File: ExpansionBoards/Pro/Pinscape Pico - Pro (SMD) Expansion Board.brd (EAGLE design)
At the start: 170.6 x 108 mm, 213 parts, among them IC1 UCC27523D, IC10 UCC27523D, IC11 UCC27523D, IC12 UCC27523D, IC13 UCC27523D, IC14 UCC27523D, IC15 TLC59116FIRHBR, IC16 TLC59116FIRHBR, IC17 TLC59116FIRHBR, IC18 TLC59116FIRHBR, IC19 ULN2803ADWR, IC2 UCC27523D, IC20 ULN2803ADWR, IC21 ULN2803ADWR, IC22 ULN2803ADWR, IC23 ULN2803ADWR, IC24 SN74HC165PWR, IC25 SN74HC165PWR, IC26 SN74HC165PWR, IC27 SN74HC165PWR, IC28 LIS3DHTR, IC29 SN74LVC1G175DCKR, IC3 UCC27523D, IC30 APX809S-29SA-7, IC31 LTV-827S, IC32 ADS1115IDGSR, IC33 TLV75733PDBVR, IC34 RV-3032-C7, IC4 UCC27523D, IC5 UCC27523D, IC6 UCC27523D, IC7 UCC27523D, IC8 UCC27523D, IC9 UCC27523D, J1 640445-6, J10 1-640456-0, J11 1-640456-0, J12 1-640456-0, J13 640445-5, J14 640445-9, J15 640445-9, J16 640445-9, J2 30316-6002HB, J3 1-640456-0, J4 640456-9, J5 640456-9, J6 640454-2, J7 215079-4, J8 30308-6002HB, J9 1-640456-0, Q1 BUK7K89-100EX, Q10 BUK7K89-100EX, Q11 BUK7K89-100EX, Q12 BUK7K89-100EX, Q13 BUK7K89-100EX, Q14 BUK7K89-100EX, Q15 UMA5NTR, Q16 UMA5NTR, Q17 UMA5NTR, Q18 UMA5NTR, Q19 UMA5NTR, Q2 BUK7K89-100EX, Q20 UMA5NTR, Q21 UMA5NTR, Q22 UMA5NTR, Q23 UMA5NTR, Q24 UMA5NTR, Q25 UMA5NTR, Q26 UMA5NTR, Q27 DSS8110Y-7, Q3 BUK7K89-100EX, Q4 BUK7K89-100EX, Q5 BUK7K89-100EX, Q6 BUK7K89-100EX, Q7 BUK7K89-100EX, Q8 BUK7K89-100EX, Q9 BUK7K89-100EX, SW1 TS-1187A-B-A-B, U1 BAT-HLD-001-THM

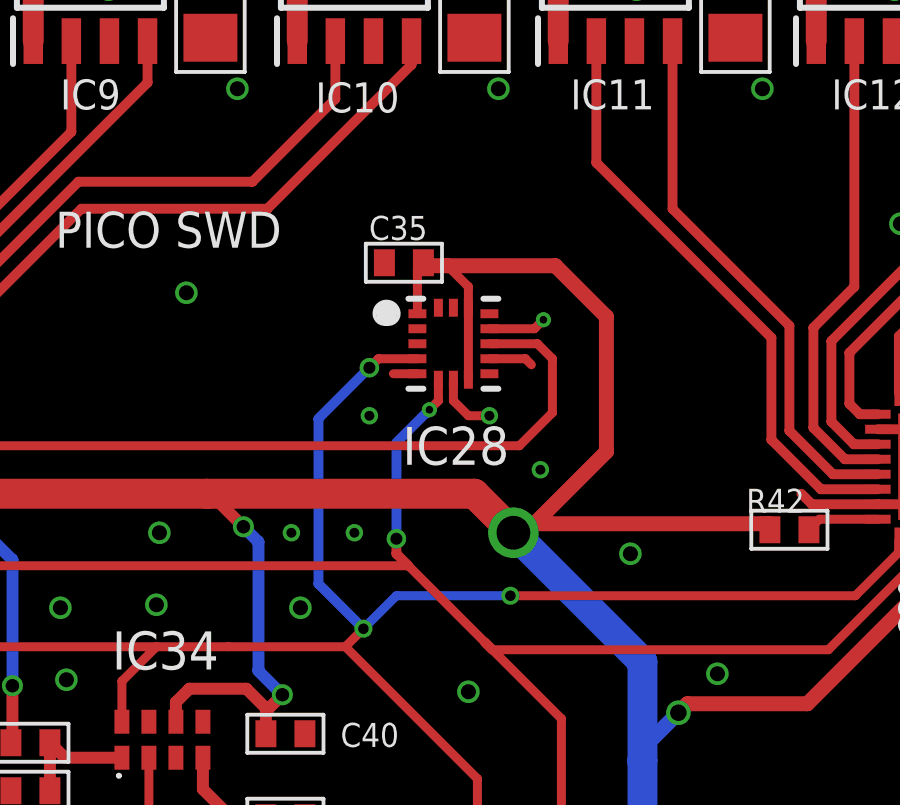
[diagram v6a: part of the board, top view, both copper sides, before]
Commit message: Update Pro and KL25Z adapter boards to make LIS3DH footprint compatible with LIS3DSH
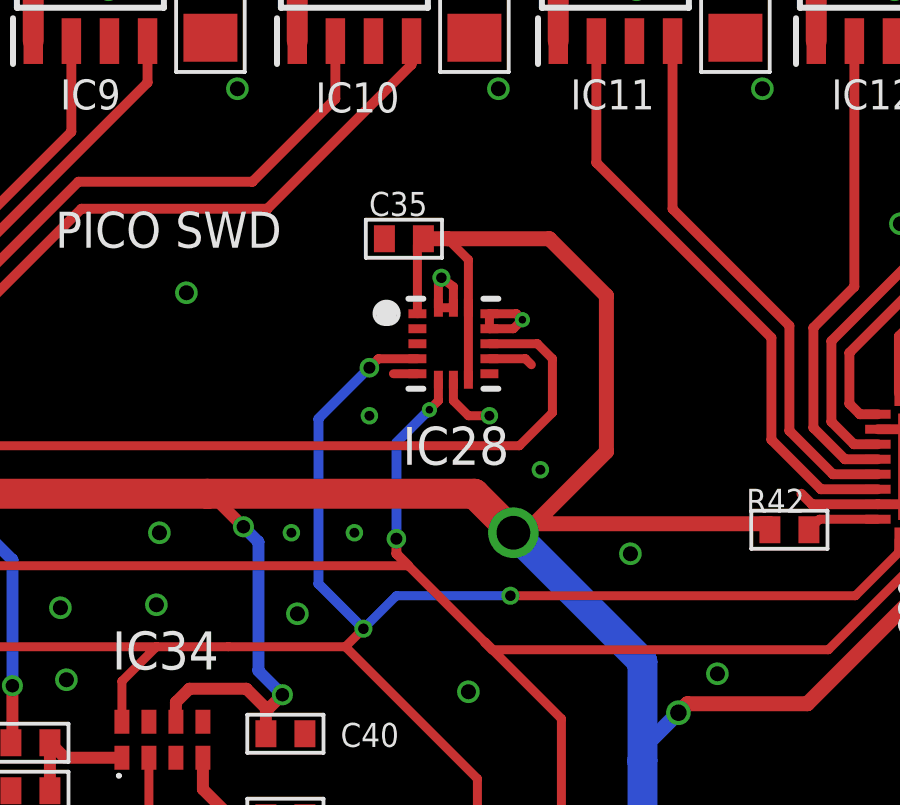
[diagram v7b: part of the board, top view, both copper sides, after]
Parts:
- moved C35 0.80 mm to (95.5, 68.4)
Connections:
- net GND: now also IC28.13, IC28.15, IC28.16
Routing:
- net GND: track 113.2 -> 117.0 mm, vias 312 -> 313
- net 3V3_PERIPHERAL: track 359.3 -> 361.7 mm
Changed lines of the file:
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@@
 <layer number="98" name="Guide" color="6" fill="1" visible="no" active="no"/>
 <layer number="99" name="SpiceOrder" color="5" fill="1" visible="no" active="no"/>
-<layer number="100" name="US-Transistor" color="7" fill="1" visible="no" active="yes"/>
-<layer number="101" name="EU-Transistor" color="7" fill="1" visible="no" active="yes"/>
+<layer number="100" name="US-Transistor" color="7" fill="1" visible="yes" active="yes"/>
+<layer number="101" name="EU-Transistor" color="7" fill="1" visible="yes" active="yes"/>
 <layer number="102" name="Vscore" color="7" fill="1" visible="no" active="yes"/>
 <layer number="103" name="fp3" color="7" fill="1" visible="no" active="yes"/>
@@
 <attribute name="VALUE" x="83.386" y="18.23" size="0.8" layer="27" rot="R90" align="center"/>
 </element>
-<element name="C35" library="rcl" package="C0402" value="0.1uF" x="95.45" y="67.6" smashed="yes" rot="R180">
-<attribute name="NAME" x="95.26" y="68.76" size="0.8" layer="25" align="center"/>
+<element name="C35" library="rcl" package="C0402" value="0.1uF" x="95.45" y="68.4" smashed="yes" rot="R180">
+<attribute name="NAME" x="95.26" y="69.56" size="0.8" layer="25" align="center"/>
 </element>
 <element name="R31" library="rcl" package="R0603" value="2R5" x="99.4" y="14.4" smashed="yes" rot="R90">
@@
 <attribute name="MOUSER_PART_NUMBER" value="511-LIS3DHTR" x="97.1" y="64.9" size="1" layer="27" ratio="15" display="off"/>
 <attribute name="NAME" x="97.181" y="61.5" size="1.27" layer="25" rot="R180" align="center"/>
-<attribute name="VALUE" x="99.4" y="65.519" size="0.7" layer="27" rot="R90" align="center"/>
+<attribute name="VALUE" x="92.881" y="65" size="0.7" layer="27" rot="R180" align="center"/>
 </element>
 <element name="IC31" library="SamacSys_Parts" package="SOP254P1016X460-8N" value="LTV-827S" x="44.1" y="37.6" smashed="yes" rot="R180">
@@
 <via x="52.5" y="14" extent="1-16" drill="0.254"/>
 <via x="94.3" y="42" extent="1-16" drill="0.5"/>
-<via x="92" y="56.1" extent="1-16" drill="0.5"/>
+<via x="91.9" y="55.9" extent="1-16" drill="0.5"/>
 <via x="105.7" y="39.9" extent="1-16" drill="0.3" diameter="0.7"/>
 <via x="101.7" y="39.8" extent="1-16" drill="0.3" diameter="0.7"/>
@@
 <via x="98.3" y="62.5" extent="1-16" drill="0.33"/>
 <via x="100" y="60.7" extent="1-16" drill="0.33"/>
-<wire x1="98.3" y1="65.4" x2="99.8" y2="65.4" width="0.3" layer="1"/>
+<wire x1="98.3" y1="65.4" x2="99.1" y2="65.4" width="0.3" layer="1"/>
 <wire x1="97.1" y1="63.7" x2="97.1" y2="63" width="0.3" layer="1"/>
 <wire x1="97.1" y1="63" x2="97.6" y2="62.5" width="0.3" layer="1"/>
-<wire x1="99.8" y1="65.4" x2="100.1" y2="65.7" width="0.3" layer="1"/>
-<via x="100.1" y="65.7" extent="1-16" drill="0.254"/>
+<wire x1="99.1" y1="65.4" x2="99.4" y2="65.7" width="0.3" layer="1"/>
+<via x="99.4" y="65.7" extent="1-16" drill="0.254"/>
 <wire x1="98.3" y1="62.5" x2="97.6" y2="62.5" width="0.3" layer="1"/>
 <contactref element="J1" pad="2"/>
@@
 <contactref element="R31" pad="1"/>
 <contactref element="D2" pad="1"/>
+<contactref element="IC28" pad="13"/>
+<contactref element="IC28" pad="15"/>
+<contactref element="IC28" pad="16"/>
+<wire x1="97.1" y1="66.1" x2="96.6" y2="66.1" width="0.3" layer="1"/>
+<via x="96.7" y="67.1" extent="1-16" drill="0.35"/>
+<wire x1="96.6" y1="66.1" x2="96.6" y2="67" width="0.3" layer="1"/>
+<wire x1="96.6" y1="67" x2="96.7" y2="67.1" width="0.3" layer="1"/>
+<wire x1="97.1" y1="66.1" x2="97.1" y2="66.8" width="0.3" layer="1"/>
+<wire x1="97.1" y1="66.8" x2="96.7" y2="67.1" width="0.3" layer="1"/>
+<wire x1="98.3" y1="65.9" x2="98.3" y2="65.4" width="0.3" layer="1"/>
+<wire x1="98.3" y1="65.9" x2="99.2" y2="65.9" width="0.3" layer="1"/>
+<wire x1="99.2" y1="65.9" x2="99.4" y2="65.7" width="0.3" layer="1"/>
 </signal>
 <signal name="5V">
@@
 <contactref element="IC28" pad="1"/>
 <contactref element="IC28" pad="14"/>
-<wire x1="97.6" y1="66.1" x2="97.6" y2="66.8" width="0.3" layer="1"/>
-<wire x1="95.9" y1="65.9" x2="95.9" y2="67.4" width="0.3" layer="1"/>
-<wire x1="95.9" y1="67.4" x2="96.1" y2="67.6" width="0.3" layer="1"/>
-<wire x1="96.1" y1="67.6" x2="96.1" y2="67.5" width="0.3" layer="1"/>
-<wire x1="102.2" y1="61.3" x2="102.2" y2="65.8" width="0.5" layer="1"/>
-<wire x1="96.1" y1="67.5" x2="96.9" y2="67.5" width="0.5" layer="1"/>
-<wire x1="96.9" y1="67.5" x2="100.5" y2="67.5" width="0.5" layer="1"/>
-<wire x1="97.6" y1="66.8" x2="96.9" y2="67.5" width="0.3" layer="1"/>
+<wire x1="95.9" y1="65.9" x2="95.9" y2="68.2" width="0.3" layer="1"/>
+<wire x1="95.9" y1="68.2" x2="96.1" y2="68.4" width="0.3" layer="1"/>
+<wire x1="102.2" y1="61.3" x2="102.2" y2="66.5" width="0.5" layer="1"/>
+<wire x1="96.1" y1="68.4" x2="96.9" y2="68.4" width="0.5" layer="1"/>
 <contactref element="R39" pad="2"/>
 <contactref element="R42" pad="2"/>
 <contactref element="R43" pad="2"/>
 <contactref element="R44" pad="2"/>
+<wire x1="96.9" y1="68.4" x2="100.3" y2="68.4" width="0.5" layer="1"/>
 <wire x1="48.05" y1="63.6" x2="48.05" y2="61.95" width="0.33" layer="1"/>
 <wire x1="109.95" y1="42.3" x2="104.4" y2="42.3" width="0.33" layer="1"/>
@@
 <contactref element="LED2" pad="2"/>
 <contactref element="IC28" pad="8"/>
-<wire x1="100.5" y1="67.5" x2="102.2" y2="65.8" width="0.5" layer="1"/>
 <wire x1="107.65" y1="58.9" x2="99.4" y2="58.9" width="0.5" layer="1"/>
 <wire x1="99.4" y1="58.9" x2="99.1" y2="58.6" width="0.5" layer="1"/>
@@
 <wire x1="40.1" y1="13.1" x2="38.59" y2="11.59" width="0.5" layer="16"/>
 <wire x1="38.59" y1="25.845675" x2="38.59" y2="38.41" width="1" layer="16"/>
+<wire x1="102.2" y1="66.5" x2="100.3" y2="68.4" width="0.5" layer="1"/>
+<wire x1="97.6" y1="66.1" x2="97.6" y2="67.7" width="0.3" layer="1"/>
+<wire x1="97.6" y1="67.7" x2="96.9" y2="68.4" width="0.3" layer="1"/>
 </signal>
 <signal name="/OUTCTL1">

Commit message: Exp boards: update gate resistors in BOMs
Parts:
- R10, R11, R12, R13, R14, R15, R16, R17, R18, R19, R20, R21, R22, R23, R24, R25, R26, R27, R28, R5, R6, R7, R8, R9: value 4R7 -> 200R
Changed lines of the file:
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@@
 <attribute name="VALUE" x="119.8" y="78.69" size="0.55" layer="27" rot="R180" align="center"/>
 </element>
-<element name="R21" library="resistor" package="R0603" value="4R7" x="101.3" y="83.1" smashed="yes" rot="R270">
+<element name="R21" library="resistor" package="R0603" value="200R" x="101.3" y="83.1" smashed="yes" rot="R270">
 <attribute name="NAME" x="101.37" y="85.284" size="0.8" layer="25" rot="R180" align="center"/>
 </element>
-<element name="R22" library="resistor" package="R0603" value="4R7" x="106.1" y="83.1" smashed="yes" rot="R270">
+<element name="R22" library="resistor" package="R0603" value="200R" x="106.1" y="83.1" smashed="yes" rot="R270">
 <attribute name="NAME" x="106.17" y="85.184" size="0.8" layer="25" rot="R180" align="center"/>
 </element>
-<element name="R23" library="resistor" package="R0603" value="4R7" x="109.9" y="83.1" smashed="yes" rot="R270">
+<element name="R23" library="resistor" package="R0603" value="200R" x="109.9" y="83.1" smashed="yes" rot="R270">
 <attribute name="NAME" x="109.87" y="85.184" size="0.8" layer="25" rot="R180" align="center"/>
 </element>
-<element name="R24" library="resistor" package="R0603" value="4R7" x="114.9" y="83.1" smashed="yes" rot="R270">
+<element name="R24" library="resistor" package="R0603" value="200R" x="114.9" y="83.1" smashed="yes" rot="R270">
 <attribute name="NAME" x="116.484" y="83.33" size="0.8" layer="25" rot="R90" align="center"/>
 </element>
-<element name="R25" library="resistor" package="R0603" value="4R7" x="118.6" y="83.1" smashed="yes" rot="R270">
+<element name="R25" library="resistor" package="R0603" value="200R" x="118.6" y="83.1" smashed="yes" rot="R270">
 <attribute name="NAME" x="118.57" y="85.184" size="0.8" layer="25" rot="R180" align="center"/>
 </element>
-<element name="R26" library="resistor" package="R0603" value="4R7" x="123.4" y="83.1" smashed="yes" rot="R270">
+<element name="R26" library="resistor" package="R0603" value="200R" x="123.4" y="83.1" smashed="yes" rot="R270">
 <attribute name="NAME" x="123.47" y="85.184" size="0.8" layer="25" rot="R180" align="center"/>
 </element>
-<element name="R27" library="resistor" package="R0603" value="4R7" x="127.3" y="83.1" smashed="yes" rot="R270">
+<element name="R27" library="resistor" package="R0603" value="200R" x="127.3" y="83.1" smashed="yes" rot="R270">
 <attribute name="NAME" x="127.37" y="85.184" size="0.8" layer="25" rot="R180" align="center"/>
 </element>
-<element name="R28" library="resistor" package="R0603" value="4R7" x="132.3" y="83.1" smashed="yes" rot="R270">
+<element name="R28" library="resistor" package="R0603" value="200R" x="132.3" y="83.1" smashed="yes" rot="R270">
 <attribute name="NAME" x="132.465" y="85.235" size="0.8" layer="25" align="center"/>
 </element>
-<element name="R13" library="resistor" package="R0603" value="4R7" x="66.5" y="83.1" smashed="yes" rot="R270">
+<element name="R13" library="resistor" package="R0603" value="200R" x="66.5" y="83.1" smashed="yes" rot="R270">
 <attribute name="NAME" x="66.37" y="85.084" size="0.8" layer="25" rot="R180" align="center"/>
 </element>
-<element name="R14" library="resistor" package="R0603" value="4R7" x="71.3" y="83.1" smashed="yes" rot="R270">
+<element name="R14" library="resistor" package="R0603" value="200R" x="71.3" y="83.1" smashed="yes" rot="R270">
 <attribute name="NAME" x="71.4" y="85.2" size="0.8" layer="25" rot="R180" align="center"/>
 </element>
-<element name="R15" library="resistor" package="R0603" value="4R7" x="75.1" y="83.1" smashed="yes" rot="R270">
+<element name="R15" library="resistor" package="R0603" value="200R" x="75.1" y="83.1" smashed="yes" rot="R270">
 <attribute name="NAME" x="75.07" y="85.184" size="0.8" layer="25" rot="R180" align="center"/>
 </element>
-<element name="R16" library="resistor" package="R0603" value="4R7" x="80" y="83.1" smashed="yes" rot="R270">
+<element name="R16" library="resistor" package="R0603" value="200R" x="80" y="83.1" smashed="yes" rot="R270">
 <attribute name="NAME" x="79.97" y="85.184" size="0.8" layer="25" rot="R180" align="center"/>
 </element>
-<element name="R17" library="resistor" package="R0603" value="4R7" x="83.9" y="83.1" smashed="yes" rot="R270">
+<element name="R17" library="resistor" package="R0603" value="200R" x="83.9" y="83.1" smashed="yes" rot="R270">
 <attribute name="NAME" x="84.07" y="85.184" size="0.8" layer="25" rot="R180" align="center"/>
 </element>
-<element name="R18" library="resistor" package="R0603" value="4R7" x="88.7" y="83.1" smashed="yes" rot="R270">
+<element name="R18" library="resistor" package="R0603" value="200R" x="88.7" y="83.1" smashed="yes" rot="R270">
 <attribute name="NAME" x="88.77" y="85.284" size="0.8" layer="25" rot="R180" align="center"/>
 </element>
-<element name="R19" library="resistor" package="R0603" value="4R7" x="92.6" y="83.1" smashed="yes" rot="R270">
+<element name="R19" library="resistor" package="R0603" value="200R" x="92.6" y="83.1" smashed="yes" rot="R270">
 <attribute name="NAME" x="92.57" y="85.184" size="0.8" layer="25" rot="R180" align="center"/>
 </element>
-<element name="R20" library="resistor" package="R0603" value="4R7" x="97.5" y="83.1" smashed="yes" rot="R270">
+<element name="R20" library="resistor" package="R0603" value="200R" x="97.5" y="83.1" smashed="yes" rot="R270">
 <attribute name="NAME" x="97.67" y="85.184" size="0.8" layer="25" rot="R180" align="center"/>
 </element>
-<element name="R5" library="resistor" package="R0603" value="4R7" x="32" y="83.1" smashed="yes" rot="R270">
+<element name="R5" library="resistor" package="R0603" value="200R" x="32" y="83.1" smashed="yes" rot="R270">
 <attribute name="NAME" x="32.165" y="85.235" size="0.8" layer="25" align="center"/>
 </element>
-<element name="R6" library="resistor" package="R0603" value="4R7" x="36.8" y="83.1" smashed="yes" rot="R270">
+<element name="R6" library="resistor" package="R0603" value="200R" x="36.8" y="83.1" smashed="yes" rot="R270">
 <attribute name="NAME" x="36.77" y="85.184" size="0.8" layer="25" rot="R180" align="center"/>
 </element>
-<element name="R7" library="resistor" package="R0603" value="4R7" x="40.4" y="83.1" smashed="yes" rot="R270">
+<element name="R7" library="resistor" package="R0603" value="200R" x="40.4" y="83.1" smashed="yes" rot="R270">
 <attribute name="NAME" x="40.77" y="85.084" size="0.8" layer="25" rot="R180" align="center"/>
 </element>
-<element name="R8" library="resistor" package="R0603" value="4R7" x="45.2" y="83.1" smashed="yes" rot="R270">
+<element name="R8" library="resistor" package="R0603" value="200R" x="45.2" y="83.1" smashed="yes" rot="R270">
 <attribute name="NAME" x="45.17" y="85.184" size="0.8" layer="25" rot="R180" align="center"/>
 </element>
-<element name="R9" library="resistor" package="R0603" value="4R7" x="49.2" y="83.1" smashed="yes" rot="R270">
+<element name="R9" library="resistor" package="R0603" value="200R" x="49.2" y="83.1" smashed="yes" rot="R270">
 <attribute name="NAME" x="49.27" y="85.084" size="0.8" layer="25" rot="R180" align="center"/>
 </element>
-<element name="R10" library="resistor" package="R0603" value="4R7" x="53.9" y="83.1" smashed="yes" rot="R270">
+<element name="R10" library="resistor" package="R0603" value="200R" x="53.9" y="83.1" smashed="yes" rot="R270">
 <attribute name="NAME" x="53.87" y="85.184" size="0.8" layer="25" rot="R180" align="center"/>
 </element>
-<element name="R11" library="resistor" package="R0603" value="4R7" x="57.6" y="83.1" smashed="yes" rot="R270">
+<element name="R11" library="resistor" package="R0603" value="200R" x="57.6" y="83.1" smashed="yes" rot="R270">
 <attribute name="NAME" x="57.67" y="85.184" size="0.8" layer="25" rot="R180" align="center"/>
 </element>
-<element name="R12" library="resistor" package="R0603" value="4R7" x="62.6" y="83.1" smashed="yes" rot="R270">
+<element name="R12" library="resistor" package="R0603" value="200R" x="62.6" y="83.1" smashed="yes" rot="R270">
 <attribute name="NAME" x="62.67" y="85.184" size="0.8" layer="25" rot="R180" align="center"/>
 </element>
